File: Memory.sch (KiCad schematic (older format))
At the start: 16 parts, among them U2 AS6C4008-55PCN, U3 AS6C4008-55PCN, U4 AS6C4008-55PCN, U5 AS6C4008-55PCN, U6 74HCT00, U7 74LS32, U8 74LS32, U9 74LS05

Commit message: rearange stuff
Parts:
- gave numbers to parts that had none: 2
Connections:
- net ~CS1: now also U11.10; no longer U11.9
- net ~CS2: now also U11.9; no longer U11.10
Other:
- moved on the sheet: U10B, U11C, U6A, U6B, U7A, U7B, U7C, U7D, U8A, U8B, U8C, U8D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

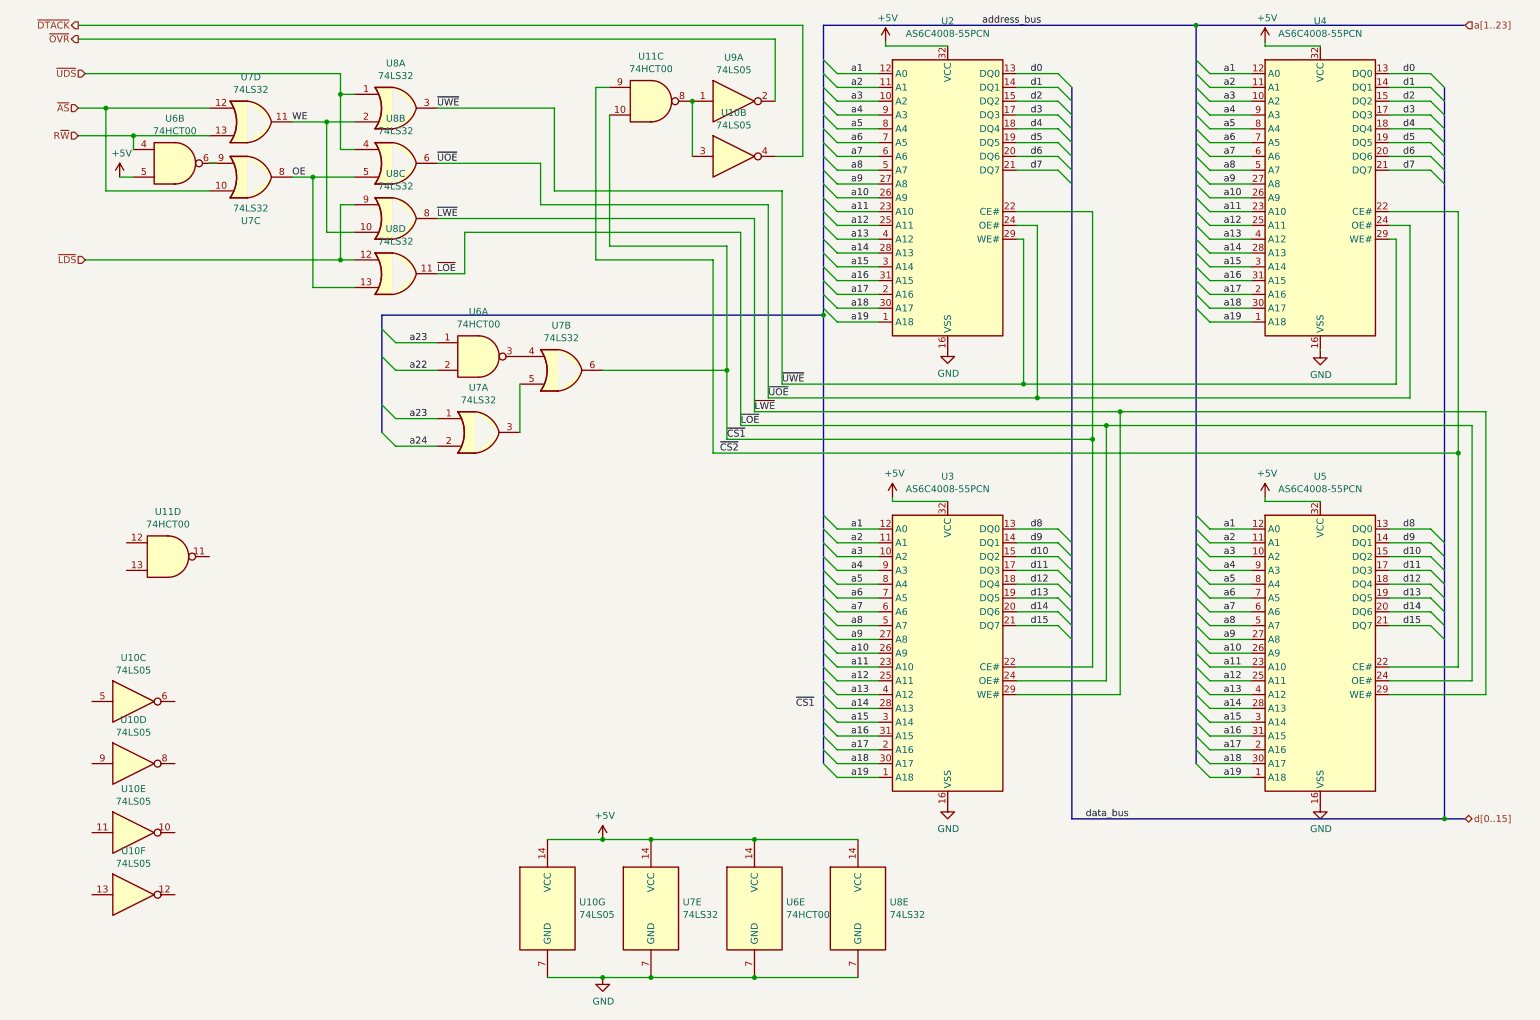
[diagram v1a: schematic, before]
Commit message: decode second bank
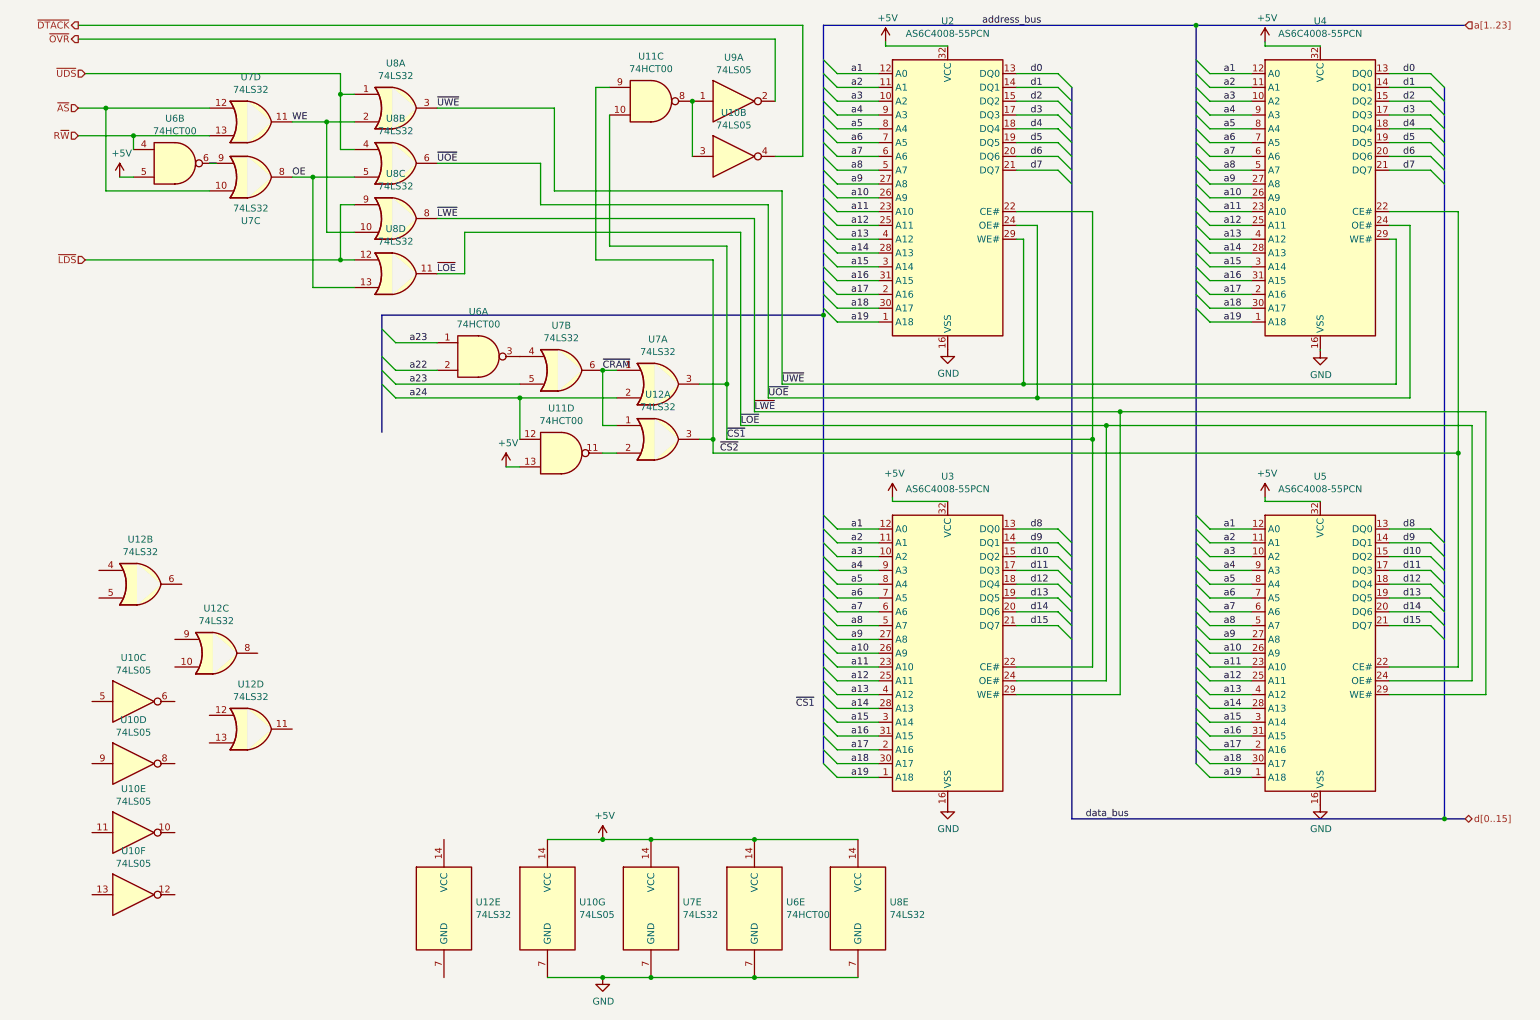
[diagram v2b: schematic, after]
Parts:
- added U12: 74LS32, symbol 74:74LS32
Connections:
- net +5V: now also U11.13
- net a23: now also U7.5; no longer U7.1
- net a24: now also U11.12
- net ~CS1: now also U7.3; no longer U7.6
- net ~CS2: now also U12.3
- net at U11.11: now also U12.2
- new net ~CRAM: U12.1, U7.1, U7.6
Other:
- moved on the sheet: U11D, U7A
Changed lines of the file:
@@
 L 74:74LS32 U7
 U 1 1 6046BC9D
-P 3700 3550
-F 0 "U7" H 3700 3875 50  0000 C CNN
-F 1 "74LS32" H 3700 3784 50  0000 C CNN
-F 2 "" H 3700 3550 50  0001 C CNN
-F 3 "http://www.ti.com/lit/gpn/sn74LS32" H 3700 3550 50  0001 C CNN
-	1    3700 3550
+P 5000 3200
+F 0 "U7" H 5000 3525 50  0000 C CNN
+F 1 "74LS32" H 5000 3434 50  0000 C CNN
+F 2 "" H 5000 3200 50  0001 C CNN
+F 3 "http://www.ti.com/lit/gpn/sn74LS32" H 5000 3200 50  0001 C CNN
+	1    5000 3200
 	1    0    0    -1
 $EndComp
@@
 $EndComp
 Wire Wire Line
-	4000 3550 4000 3200
-Wire Wire Line
 	3100 2900 3400 2900
 Wire Wire Line
 	3400 3100 3100 3100
-Wire Wire Line
-	3400 3450 3100 3450
-Wire Wire Line
-	3400 3650 3100 3650
 Text Label 3200 2900 0    50   ~ 0
 a23
 Text Label 3200 3100 0    50   ~ 0
 a22
-Text Label 3200 3450 0    50   ~ 0
+Text Label 3200 3200 0    50   ~ 0
 a23
-Text Label 3200 3650 0    50   ~ 0
-a24
 Entry Wire Line
 	3000 2800 3100 2900
 Entry Wire Line
 	3000 3000 3100 3100
-Entry Wire Line
-	3000 3350 3100 3450
-Entry Wire Line
-	3000 3550 3100 3650
 $Comp
 L 74:74HCT00 U6
@@
 F 3 "http://www.ti.com/lit/gpn/sn74hct00" H 5700 7000 50  0001 C CNN
 	5    5700 7000
-	1    0    0    -1
-$EndComp
-$Comp
-L 74:74LS32 U7
-U 5 1 6063BBA1
-P 4950 7000
-F 0 "U7" H 5180 7046 50  0000 L CNN
-F 1 "74LS32" H 5180 6955 50  0000 L CNN
-F 2 "" H 4950 7000 50  0001 C CNN
-F 3 "http://www.ti.com/lit/gpn/sn74LS32" H 4950 7000 50  0001 C CNN
-	5    4950 7000
-	1    0    0    -1
-$EndComp
-$Comp
-L OpenAmiga2000CoproAdapter-rescue:+5V-power #PWR?
-U 1 1 6069C057
-P 4600 6500
-AR Path="/6069C057" Ref="#PWR?"  Part="1"
-AR Path="/6068F728/6069C057" Ref="#PWR0110"  Part="1"
-F 0 "#PWR0110" H 4600 6350 50  0001 C CNN
-F 1 "+5V" H 4615 6673 50  0000 C CNN
-F 2 "" H 4600 6500 50  0001 C CNN
-F 3 "" H 4600 6500 50  0001 C CNN
-	1    4600 6500
 	1    0    0    -1
 $EndComp
@@
 ~LOE
 Wire Wire Line
-	4600 6500 4950 6500
-Connection ~ 4950 6500
-Wire Wire Line
 	4950 6500 5700 6500
 Connection ~ 5700 6500
 Wire Wire Line
 	5700 6500 6450 6500
-Wire Wire Line
-	4600 7500 4950 7500
-Connection ~ 4950 7500
-Wire Wire Line
-	4950 7500 5700 7500
 Connection ~ 5700 7500
 Wire Wire Line
@@
 	1    0    0    -1
 $EndComp
-Wire Wire Line
-	4200 6500 4600 6500
-Connection ~ 4600 6500
 Wire Wire Line
 	4200 7500 4600 7500
@@
 L 74:74HCT00 U11
 U 4 1 6142508F
-P 1450 4450
-F 0 "U11" H 1450 4775 50  0000 C CNN
-F 1 "74HCT00" H 1450 4684 50  0000 C CNN
-F 2 "" H 1450 4450 50  0001 C CNN
-F 3 "http://www.ti.com/lit/gpn/sn74hct00" H 1450 4450 50  0001 C CNN
-	4    1450 4450
+P 4300 3700
+F 0 "U11" H 4300 4025 50  0000 C CNN
+F 1 "74HCT00" H 4300 3934 50  0000 C CNN
+F 2 "" H 4300 3700 50  0001 C CNN
+F 3 "http://www.ti.com/lit/gpn/sn74hct00" H 4300 3700 50  0001 C CNN
+	4    4300 3700
 	1    0    0    -1
 $EndComp
@@
 	3600 2100 3600 2400
 Wire Wire Line
-	5500 3600 5500 3100
-Wire Wire Line
 	5500 2200 4650 2200
 Wire Wire Line
@@
 	5500 3600 8150 3600
 Wire Wire Line
-	5400 3700 5400 2300
+	5400 3700 5400 3600
 Wire Wire Line
 	5400 2300 4550 2300
@@
 	3000 2700 6200 2700
 Connection ~ 6200 2700
-Wire Wire Line
-	4600 3100 5500 3100
+Entry Wire Line
+	3000 3100 3100 3200
+Entry Wire Line
+	3000 3200 3100 3300
+Text Label 3200 3300 0    50   ~ 0
+a24
+Wire Wire Line
+	3100 3200 4000 3200
+Text Label 4600 3100 0    50   ~ 0
+~CRAM
+$Comp
+L 74:74LS32 U12
+U 1 1 617166E0
+P 5000 3600
+F 0 "U12" H 5000 3925 50  0000 C CNN
+F 1 "74LS32" H 5000 3834 50  0000 C CNN
+F 2 "" H 5000 3600 50  0001 C CNN
+F 3 "http://www.ti.com/lit/gpn/sn74LS32" H 5000 3600 50  0001 C CNN
+	1    5000 3600
+	1    0    0    -1
+$EndComp
+$Comp
+L 74:74LS32 U12
+U 5 1 6171C77F
+P 3450 7000
+F 0 "U12" H 3680 7046 50  0000 L CNN
+F 1 "74LS32" H 3680 6955 50  0000 L CNN
+F 2 "" H 3450 7000 50  0001 C CNN
+F 3 "http://www.ti.com/lit/gpn/sn74LS32" H 3450 7000 50  0001 C CNN
+	5    3450 7000
+	1    0    0    -1
+$EndComp
+$Comp
+L 74:74LS32 U12
+U 2 1 617205A3
+P 1250 4650
+F 0 "U12" H 1250 4975 50  0000 C CNN
+F 1 "74LS32" H 1250 4884 50  0000 C CNN
+F 2 "" H 1250 4650 50  0001 C CNN
+F 3 "http://www.ti.com/lit/gpn/sn74LS32" H 1250 4650 50  0001 C CNN
+	2    1250 4650
+	1    0    0    -1
+$EndComp
+$Comp
+L 74:74LS32 U12
+U 3 1 6172422D
+P 1800 5150
+F 0 "U12" H 1800 5475 50  0000 C CNN
+F 1 "74LS32" H 1800 5384 50  0000 C CNN
+F 2 "" H 1800 5150 50  0001 C CNN
+F 3 "http://www.ti.com/lit/gpn/sn74LS32" H 1800 5150 50  0001 C CNN
+	3    1800 5150
+	1    0    0    -1
+$EndComp
+$Comp
+L 74:74LS32 U12
+U 4 1 6172762E
+P 2050 5700
+F 0 "U12" H 2050 6025 50  0000 C CNN
+F 1 "74LS32" H 2050 5934 50  0000 C CNN
+F 2 "" H 2050 5700 50  0001 C CNN
+F 3 "http://www.ti.com/lit/gpn/sn74LS32" H 2050 5700 50  0001 C CNN
+	4    2050 5700
+	1    0    0    -1
+$EndComp
+Wire Wire Line
+	5500 2200 5500 3200
+Wire Wire Line
+	5300 3200 5500 3200
+Connection ~ 5500 3200
+Wire Wire Line
+	5500 3200 5500 3600
+Wire Wire Line
+	3100 3300 4000 3300
+Wire Wire Line
+	4600 3100 4700 3100
+Wire Wire Line
+	5300 3600 5400 3600
+Connection ~ 5400 3600
+Wire Wire Line
+	5400 3600 5400 2300
+Wire Wire Line
+	4700 3500 4600 3500
+Wire Wire Line
+	4600 3500 4600 3100
+Connection ~ 4600 3100
+Wire Wire Line
+	4600 3700 4700 3700
+Wire Wire Line
+	4000 3600 4000 3300
+Connection ~ 4000 3300
+Wire Wire Line
+	4000 3300 4700 3300
+Connection ~ 4950 7500
+Wire Wire Line
+	4950 7500 5700 7500
+Wire Wire Line
+	4600 7500 4950 7500
+Connection ~ 4950 6500
+Connection ~ 4600 6500
+Wire Wire Line
+	4200 6500 4600 6500
+Wire Wire Line
+	4600 6500 4950 6500
+$Comp
+L OpenAmiga2000CoproAdapter-rescue:+5V-power #PWR?
+U 1 1 6069C057
+P 4600 6500
+AR Path="/6069C057" Ref="#PWR?"  Part="1"
+AR Path="/6068F728/6069C057" Ref="#PWR0110"  Part="1"
+F 0 "#PWR0110" H 4600 6350 50  0001 C CNN
+F 1 "+5V" H 4615 6673 50  0000 C CNN
+F 2 "" H 4600 6500 50  0001 C CNN
+F 3 "" H 4600 6500 50  0001 C CNN
+	1    4600 6500
+	1    0    0    -1
+$EndComp
+$Comp
+L 74:74LS32 U7
+U 5 1 6063BBA1
+P 4950 7000
+F 0 "U7" H 5180 7046 50  0000 L CNN
+F 1 "74LS32" H 5180 6955 50  0000 L CNN
+F 2 "" H 4950 7000 50  0001 C CNN
+F 3 "http://www.ti.com/lit/gpn/sn74LS32" H 4950 7000 50  0001 C CNN
+	5    4950 7000
+	1    0    0    -1
+$EndComp
+$Comp
+L OpenAmiga2000CoproAdapter-rescue:+5V-power #PWR?
+U 1 1 618149E0
+P 3900 3800
+AR Path="/618149E0" Ref="#PWR?"  Part="1"
+AR Path="/6068F728/618149E0" Ref="#PWR0112"  Part="1"
+F 0 "#PWR0112" H 3900 3650 50  0001 C CNN
+F 1 "+5V" H 3915 3973 50  0000 C CNN
+F 2 "" H 3900 3800 50  0001 C CNN
+F 3 "" H 3900 3800 50  0001 C CNN
+	1    3900 3800
+	1    0    0    -1
+$EndComp
+Wire Wire Line
+	3900 3800 4000 3800
 Wire Bus Line
 	3000 2700 3000 3550
@@
 Wire Bus Line
 	8900 600  8900 5950
-Connection ~ 5500 3100
-Wire Wire Line
-	5500 3100 5500 2200
 $EndSCHEMATC

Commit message: rom emulation bank
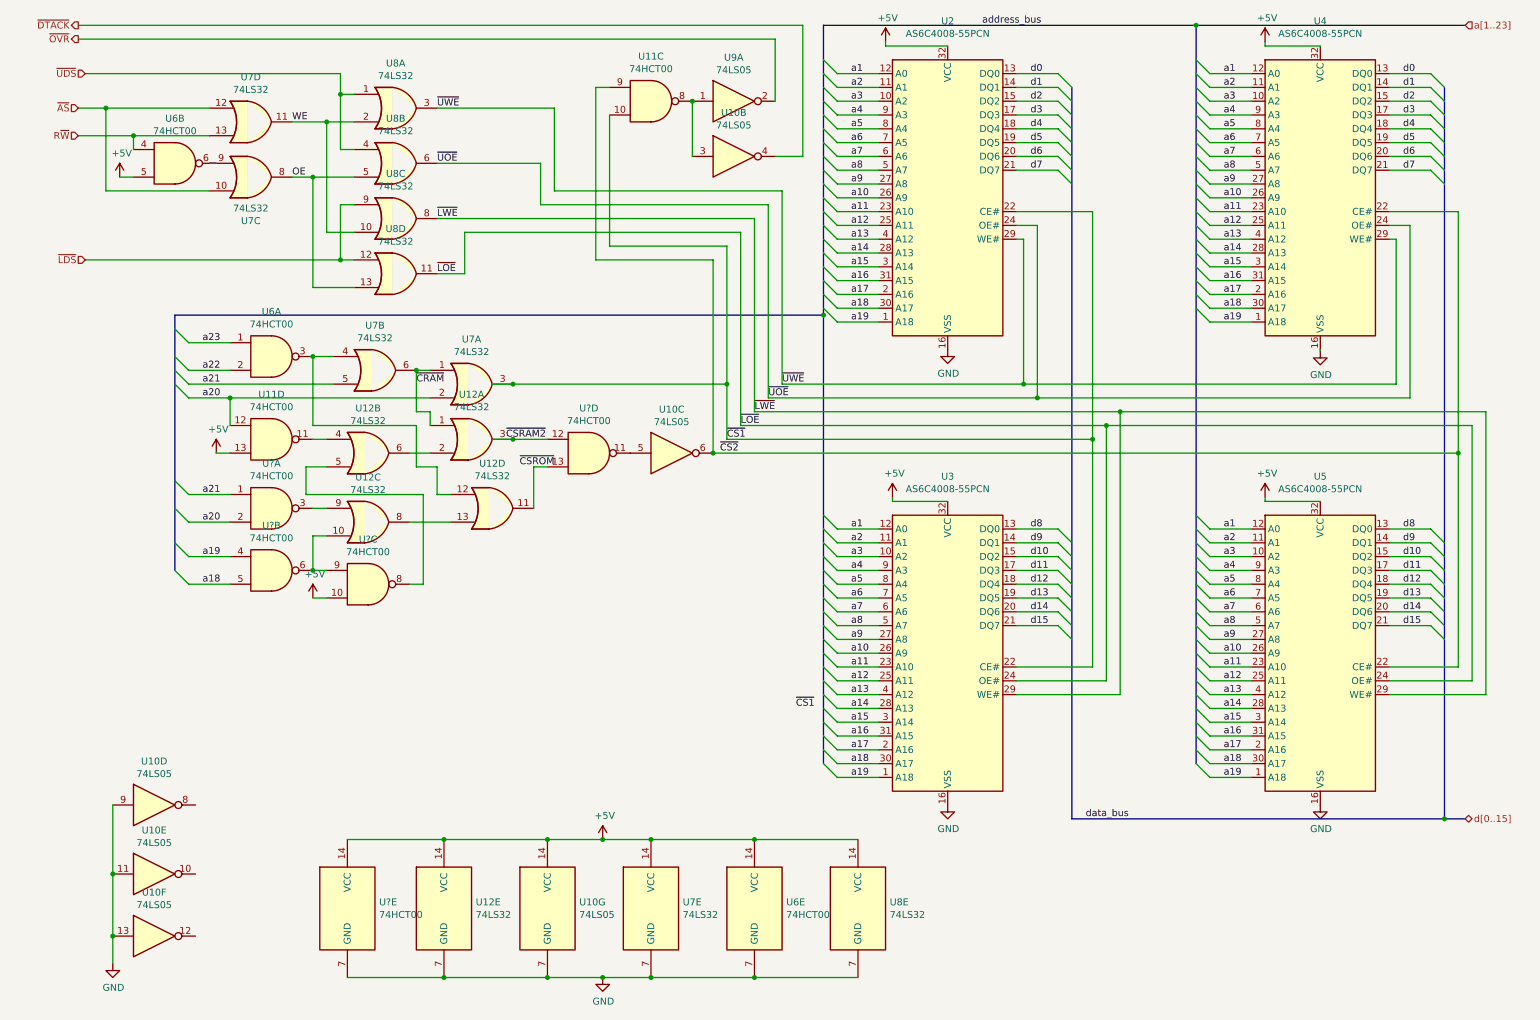
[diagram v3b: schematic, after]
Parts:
- added U? (x5): 74HCT00, symbol 74:74HCT00
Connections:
- net +5V: now also U12.14 (VCC), U?.10, U?.14 (VCC)
- net GND: now also U10.11, U10.13, U10.9, U12.7 (GND), U?.7 (GND)
- net a18: now also U?.5
- net a19: now also U?.4
- net a23: no longer U7.5
- net ~CS2: now also U10.6; no longer U12.3
- net at U6.3, U7.4: now also U12.12
- net at U10.5: now also U?.11
- net at U11.11: now also U12.4; no longer U12.2
- net at U12.5: now also U?.8
- net at U12.6: now also U12.2
- net at U12.10: now also U?.6, U?.9
- net at U12.8: now also U12.13
- net at U12.9: now also U?.3
- net at U12.11: now also U?.13
- net a24 renamed a20
- net a20: now also U?.2
- new net a21: U7.5, U?.1
- new net ~CSRAM2: U12.3, U?.12
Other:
- moved on the sheet: U10C, U10D, U10E, U10F, U11D, U12A, U12B, U12C, U12D, U6A, U7A, U7B
